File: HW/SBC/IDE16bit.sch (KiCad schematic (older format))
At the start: 13 parts, among them P1 IDE0, U15 74LS32, U16 74LS139, U17 74HC74, U18 74LS08, U19 74LS574, U20 74LS574, U21 74HC245

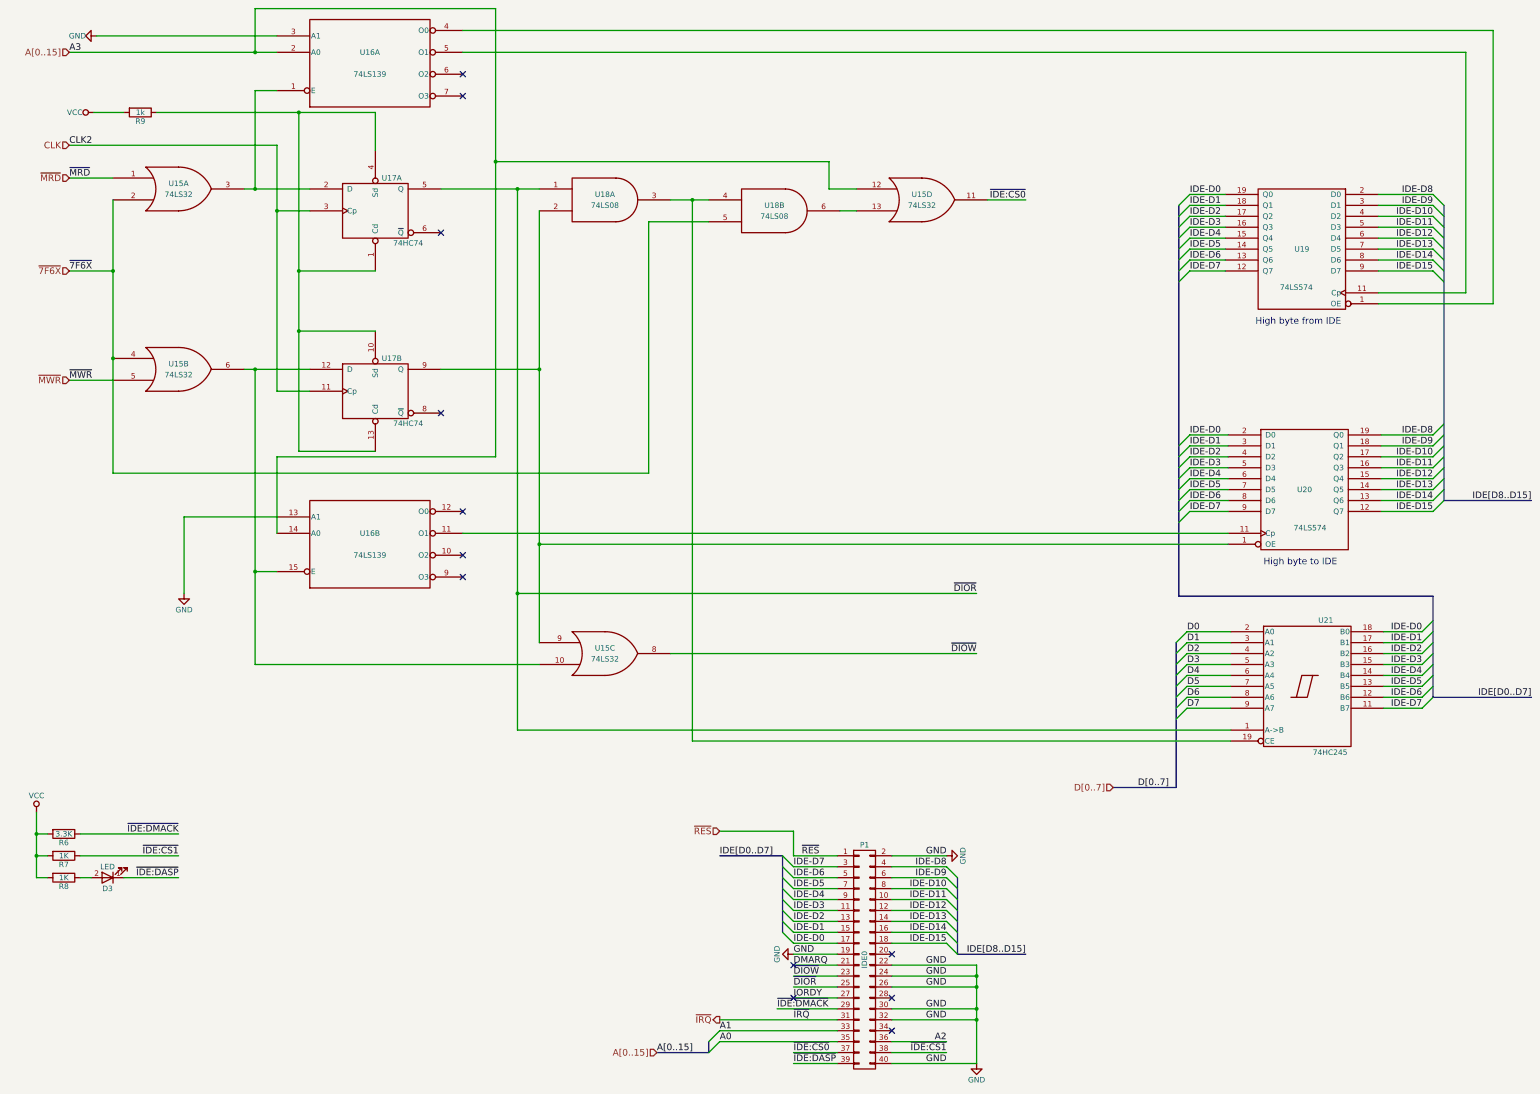
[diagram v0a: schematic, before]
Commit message: Added CPLD to schematics. Updates rest of schematics to use CPLD
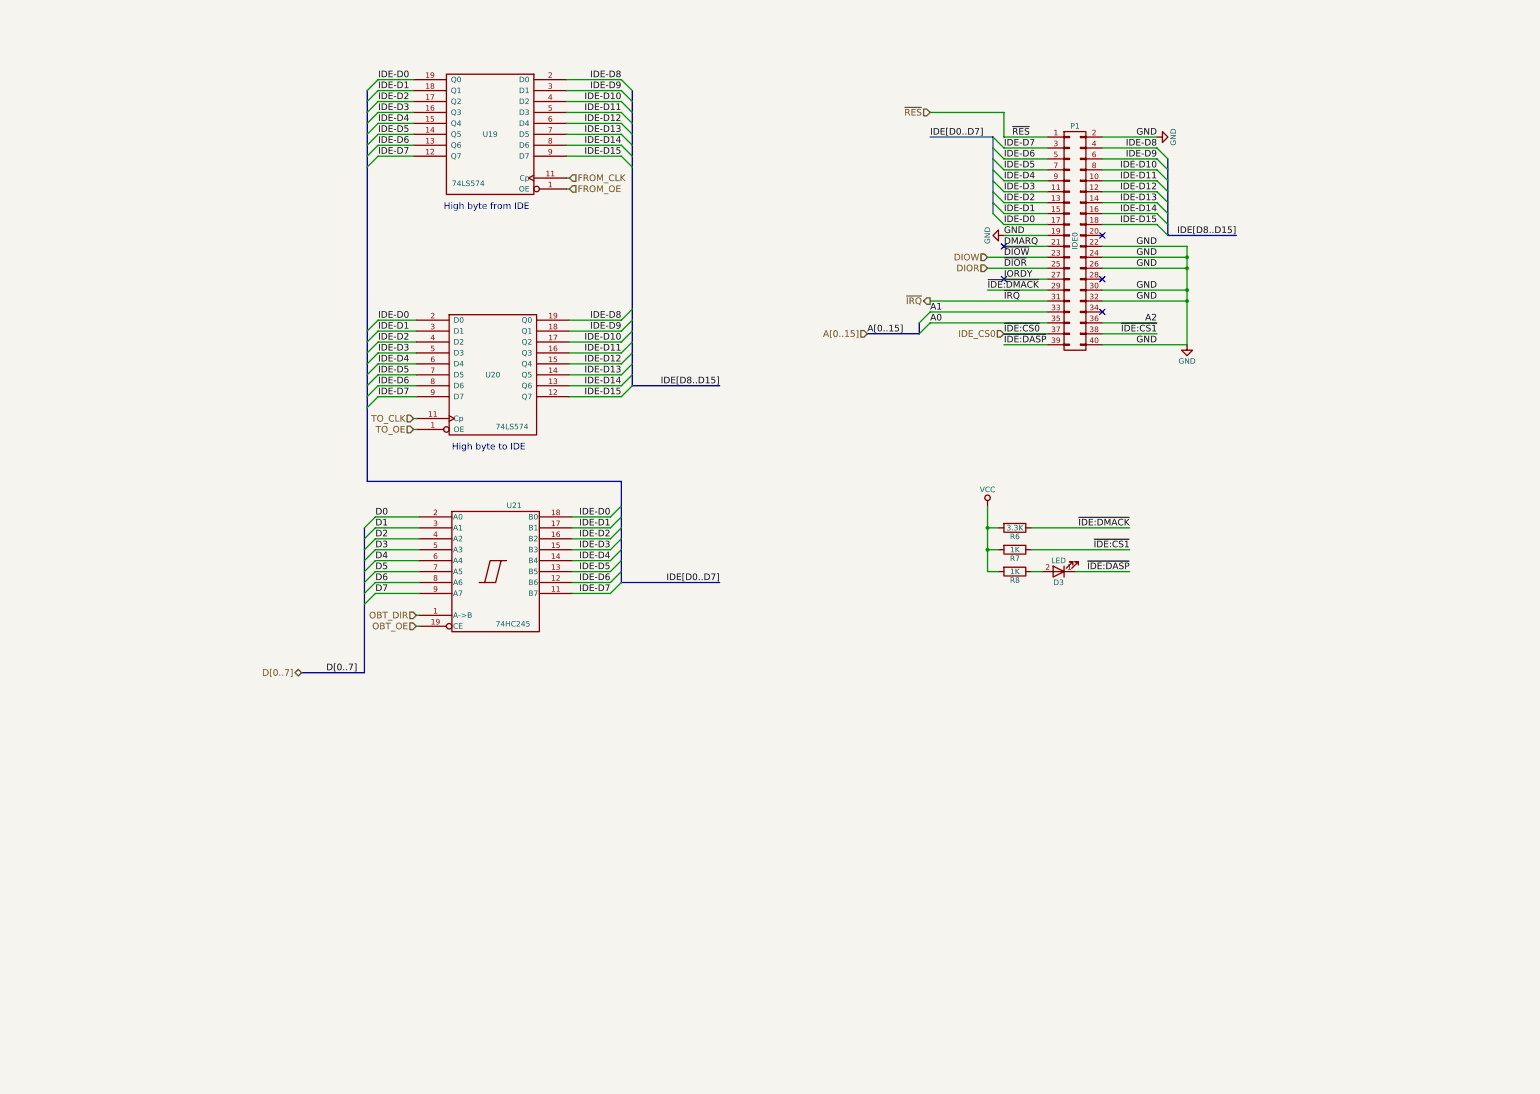
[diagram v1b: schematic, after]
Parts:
- removed R9: 1k, Resistors_ThroughHole:R_Axial_DIN0411_L9.9mm_D3.6mm_P12.70mm_Horizontal, symbol R
- removed U15: 74LS32, Housings_DIP:DIP-14_W7.62mm_Socket, symbol 74LS32
- removed U16: 74LS139, Housings_DIP:DIP-16_W7.62mm_Socket, symbol 74LS139
- removed U17: 74HC74, Housings_DIP:DIP-14_W7.62mm_Socket, symbol 74HC74
- removed U18: 74LS08, Housings_DIP:DIP-14_W7.62mm_Socket, symbol 74LS08
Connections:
- net TO_OE: now reaches U20.1 (OE)
- net FROM_OE: now reaches U19.1 (OE)
- net FROM_CLK: now reaches U19.11 (Cp)
- net TO_CLK: now reaches U20.11 (Cp)
- net OBT_OE: now reaches U21.19 (CE)
- net ~DIOR renamed DIOR
- net DIOR: no longer U21.1 (A->B)
- net ~DIOW renamed DIOW
- net ~IDE:CS0 renamed IDE_CS0
- new net OBT_DIR: U21.1 (A->B)
- no-connect marks 12 -> 5
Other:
- moved on the sheet: D3, P1, R6, R7, R8, U19, U20, U21
